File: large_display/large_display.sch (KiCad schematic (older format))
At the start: 128 parts, among them J1 Conn_01x11, J2 Conn_01x11, U1 TLC5940PWP

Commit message: routing: first pass done
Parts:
- gave numbers to parts that had none: 1
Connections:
- net GND: now also C3.2
- net Vdrive: now also C3.1
- net at Df4.1 (K), U1.12 (OUT5): now also Df7.1 (K)
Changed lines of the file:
@@
 $EndComp
 Wire Wire Line
-	2400 1500 2400 1750
+	2400 1500 2400 1600
 $Comp
 L power:GND #PWR0108
@@
 $EndComp
 Wire Wire Line
-	2400 2050 2400 2250
+	2400 2050 2400 2150
 $Comp
 L Device:R R2
@@
 $EndComp
 Wire Wire Line
-	4950 2750 4950 2800
-Wire Wire Line
 	4950 2400 4950 2450
 Wire Wire Line
@@
 	4800 3200 4950 3200
 Wire Wire Line
-	4950 3200 4950 3100
-Wire Wire Line
 	4950 3200 4950 4300
 Wire Wire Line
@@
 	7550 2400 7550 5100
 $Comp
-L Device:C C?
+L Device:C C3
 U 1 1 615CD222
 P 2750 1900
-F 0 "C?" H 2865 1946 50  0000 L CNN
+F 0 "C3" H 2865 1946 50  0000 L CNN
 F 1 "C" H 2865 1855 50  0000 L CNN
 F 2 "Capacitor_SMD:C_0805_2012Metric" H 2788 1750 50  0001 C CNN
@@
 	1    0    0    -1
 $EndComp
+Wire Wire Line
+	2400 1600 2750 1600
+Wire Wire Line
+	2750 1600 2750 1750
+Connection ~ 2400 1600
+Wire Wire Line
+	2400 1600 2400 1750
+Wire Wire Line
+	2400 2150 2750 2150
+Wire Wire Line
+	2750 2150 2750 2050
+Connection ~ 2400 2150
+Wire Wire Line
+	2400 2150 2400 2250
+Wire Wire Line
+	4950 2750 4950 3200
 $EndSCHEMATC

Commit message: Reverse Rg4 Reduce resistor size to 1206 Tidy up tracking Increase track width for VLED Fix text Add revision number
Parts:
- added R17, R22, R37, R39: R, Resistor_SMD:R_1206_3216Metric_Pad1.42x1.75mm_HandSolder, symbol Device:R
- C1, C3: value C -> 100n
- C2: value CP -> 10u
- R10, R11, R12, R13, R14, R15, R16, R3, R4, R5, R6, R7, R8, R9: footprint Resistor_SMD:R_1812_4532Metric_Pad1.30x3.40mm_HandSolder -> Resistor_SMD:R_1206_3216Metric_Pad1.42x1.75mm_HandSolder
- R18: renamed from R17; footprint Resistor_SMD:R_1812_4532Metric_Pad1.30x3.40mm_HandSolder -> Resistor_SMD:R_1206_3216Metric_Pad1.42x1.75mm_HandSolder
- R19: renamed from R18; footprint Resistor_SMD:R_1812_4532Metric_Pad1.30x3.40mm_HandSolder -> Resistor_SMD:R_1206_3216Metric_Pad1.42x1.75mm_HandSolder
- R2: value R -> 100k
- R20: renamed from R19; footprint Resistor_SMD:R_1812_4532Metric_Pad1.30x3.40mm_HandSolder -> Resistor_SMD:R_1206_3216Metric_Pad1.42x1.75mm_HandSolder
- R21: renamed from R20; footprint Resistor_SMD:R_1812_4532Metric_Pad1.30x3.40mm_HandSolder -> Resistor_SMD:R_1206_3216Metric_Pad1.42x1.75mm_HandSolder
- R23: renamed from R21; footprint Resistor_SMD:R_1812_4532Metric_Pad1.30x3.40mm_HandSolder -> Resistor_SMD:R_1206_3216Metric_Pad1.42x1.75mm_HandSolder
- R24: renamed from R22; footprint Resistor_SMD:R_1812_4532Metric_Pad1.30x3.40mm_HandSolder -> Resistor_SMD:R_1206_3216Metric_Pad1.42x1.75mm_HandSolder
- R25: renamed from R23; footprint Resistor_SMD:R_1812_4532Metric_Pad1.30x3.40mm_HandSolder -> Resistor_SMD:R_1206_3216Metric_Pad1.42x1.75mm_HandSolder
- R26: renamed from R24; footprint Resistor_SMD:R_1812_4532Metric_Pad1.30x3.40mm_HandSolder -> Resistor_SMD:R_1206_3216Metric_Pad1.42x1.75mm_HandSolder
- R27: renamed from R25; footprint Resistor_SMD:R_1812_4532Metric_Pad1.30x3.40mm_HandSolder -> Resistor_SMD:R_1206_3216Metric_Pad1.42x1.75mm_HandSolder
- R28: renamed from R26; footprint Resistor_SMD:R_1812_4532Metric_Pad1.30x3.40mm_HandSolder -> Resistor_SMD:R_1206_3216Metric_Pad1.42x1.75mm_HandSolder
- R29: renamed from R27; footprint Resistor_SMD:R_1812_4532Metric_Pad1.30x3.40mm_HandSolder -> Resistor_SMD:R_1206_3216Metric_Pad1.42x1.75mm_HandSolder
- R30: renamed from R28; footprint Resistor_SMD:R_1812_4532Metric_Pad1.30x3.40mm_HandSolder -> Resistor_SMD:R_1206_3216Metric_Pad1.42x1.75mm_HandSolder
- R31: renamed from R29; footprint Resistor_SMD:R_1812_4532Metric_Pad1.30x3.40mm_HandSolder -> Resistor_SMD:R_1206_3216Metric_Pad1.42x1.75mm_HandSolder
- R32: renamed from R30; footprint Resistor_SMD:R_1812_4532Metric_Pad1.30x3.40mm_HandSolder -> Resistor_SMD:R_1206_3216Metric_Pad1.42x1.75mm_HandSolder
- R33: renamed from R31; footprint Resistor_SMD:R_1812_4532Metric_Pad1.30x3.40mm_HandSolder -> Resistor_SMD:R_1206_3216Metric_Pad1.42x1.75mm_HandSolder
- R34: renamed from R32; footprint Resistor_SMD:R_1812_4532Metric_Pad1.30x3.40mm_HandSolder -> Resistor_SMD:R_1206_3216Metric_Pad1.42x1.75mm_HandSolder
- R35: renamed from R33; footprint Resistor_SMD:R_1812_4532Metric_Pad1.30x3.40mm_HandSolder -> Resistor_SMD:R_1206_3216Metric_Pad1.42x1.75mm_HandSolder
- R36: renamed from R34; footprint Resistor_SMD:R_1812_4532Metric_Pad1.30x3.40mm_HandSolder -> Resistor_SMD:R_1206_3216Metric_Pad1.42x1.75mm_HandSolder
- R38: renamed from R35; footprint Resistor_SMD:R_1812_4532Metric_Pad1.30x3.40mm_HandSolder -> Resistor_SMD:R_1206_3216Metric_Pad1.42x1.75mm_HandSolder
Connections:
- net Vdrive: now also R17.1; no longer R18.1
- net at R20.2, U1.14 (OUT7): now also R22.2; no longer R21.2
- net at Dg3.2 (A), R18.2: now also Dg4.1 (K); no longer Dg4.2 (A)
- net at R19.1: now also Dg4.2 (A); no longer Dg4.1 (K)
- net at R36.2: now also R37.1; no longer Dn3.2 (A)
- net at R38.2: now also R39.1; no longer Dp1.2 (A)
- new net: R17.2, R18.1
- new net: Dn3.2 (A), R37.2
- new net: Dp1.2 (A), R39.2
- new net: R21.2, R22.1
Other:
- moved on the sheet: Dg3, Dg4, Dn3, Dp1, R16, R18, R19, R20, R21

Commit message: Add buffering for passthru signals More tidying up of tracking
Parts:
- added U2: 74HC244, symbol 74xx:74HC244
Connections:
- net GND: now also U2.1 (1OE), U2.10 (GND), U2.19 (2OE), U2.4 (1A1), U2.6 (1A2)
- net VCC: now also U2.20 (VCC)
- net at J2.5 (Pin_5), U1.2 (BLANK): now also U2.17 (2A0); no longer J1.5 (Pin_5)
- net at J2.4 (Pin_4), U1.25 (GSCLK): now also U2.8 (1A3); no longer J1.4 (Pin_4)
- net at J2.1 (Pin_1), R2.2, U1.26 (DCPRG): now also U2.2 (1A0); no longer J1.1 (Pin_1)
- net at J2.6 (Pin_6), U1.3 (XLAT): now also U2.15 (2A1); no longer J1.6 (Pin_6)
- net at J2.7 (Pin_7), U1.4 (SCLK): now also U2.13 (2A2); no longer J1.7 (Pin_7)
- net at U1.5 (SIN): now also U2.11 (2A3); no longer J1.8 (Pin_8)
- new net: J1.1 (Pin_1), U2.18 (1Y0)
- new net: J1.4 (Pin_4), U2.12 (1Y3)
- new net: J1.5 (Pin_5), U2.3 (2Y0)
- new net: J1.6 (Pin_6), U2.5 (2Y1)
- new net: J1.7 (Pin_7), U2.7 (2Y2)
- new net: J1.8 (Pin_8), U2.9 (2Y3)
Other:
- moved on the sheet: J1
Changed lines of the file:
@@
 $EndComp
-Wire Wire Line
-	9050 2950 8950 2950
 Wire Wire Line
 	8800 4900 9050 4900
@@
 L power:VCC #PWR010
 U 1 1 5FBCAFFD
-P 8700 1750
-F 0 "#PWR010" H 8700 1600 50  0001 C CNN
-F 1 "VCC" H 8717 1923 50  0000 C CNN
-F 2 "" H 8700 1750 50  0001 C CNN
-F 3 "" H 8700 1750 50  0001 C CNN
-	1    8700 1750
+P 8700 1400
+F 0 "#PWR010" H 8700 1250 50  0001 C CNN
+F 1 "VCC" H 8717 1573 50  0000 C CNN
+F 2 "" H 8700 1400 50  0001 C CNN
+F 3 "" H 8700 1400 50  0001 C CNN
+	1    8700 1400
 	1    0    0    -1
 $EndComp
@@
 L power:Vdrive #PWR011
 U 1 1 5FBCC6DE
-P 8950 1750
-F 0 "#PWR011" H 8750 1600 50  0001 C CNN
-F 1 "Vdrive" H 8967 1923 50  0000 C CNN
-F 2 "" H 8950 1750 50  0001 C CNN
-F 3 "" H 8950 1750 50  0001 C CNN
-	1    8950 1750
+P 8800 1150
+F 0 "#PWR011" H 8600 1000 50  0001 C CNN
+F 1 "Vdrive" H 8817 1323 50  0000 C CNN
+F 2 "" H 8800 1150 50  0001 C CNN
+F 3 "" H 8800 1150 50  0001 C CNN
+	1    8800 1150
 	1    0    0    -1
 $EndComp
@@
 L Connector_Generic:Conn_01x11 J1
 U 1 1 5FC1A142
-P 9250 2450
-F 0 "J1" H 9330 2492 50  0000 L CNN
-F 1 "Conn_01x11" H 9330 2401 50  0000 L CNN
-F 2 "Connector_PinHeader_2.54mm:PinHeader_1x11_P2.54mm_Horizontal" H 9250 2450 50  0001 C CNN
-F 3 "~" H 9250 2450 50  0001 C CNN
-	1    9250 2450
+P 10600 2450
+F 0 "J1" H 10680 2492 50  0000 L CNN
+F 1 "Conn_01x11" H 10680 2401 50  0000 L CNN
+F 2 "Connector_PinHeader_2.54mm:PinHeader_1x11_P2.54mm_Horizontal" H 10600 2450 50  0001 C CNN
+F 3 "~" H 10600 2450 50  0001 C CNN
+	1    10600 2450
 	1    0    0    -1
 $EndComp
@@
 $EndComp
 Wire Wire Line
-	8950 1750 8950 2950
-Wire Wire Line
-	9050 2850 8750 2850
-Wire Wire Line
-	8750 2850 8750 4800
-Wire Wire Line
-	8800 2950 8800 4900
-Wire Wire Line
-	9050 2750 8700 2750
-Wire Wire Line
-	8700 2750 8700 4700
-Wire Wire Line
 	8700 4700 9050 4700
 Wire Wire Line
-	9050 2550 8550 2550
-Wire Wire Line
 	8550 2550 8550 4500
 Wire Wire Line
 	8550 4500 9050 4500
 Wire Wire Line
-	9050 2450 8500 2450
-Wire Wire Line
 	8500 2450 8500 4400
 Wire Wire Line
 	8500 4400 9050 4400
 Wire Wire Line
-	9050 2350 8450 2350
-Wire Wire Line
 	8450 2350 8450 4300
 Wire Wire Line
 	8450 4300 9050 4300
 Wire Wire Line
-	9050 2250 8400 2250
-Wire Wire Line
 	8400 2250 8400 4200
 Wire Wire Line
 	8400 4200 9050 4200
 Wire Wire Line
-	9050 2150 8350 2150
-Wire Wire Line
-	8350 2150 8350 4100
-Wire Wire Line
 	8350 4100 9050 4100
 Wire Wire Line
-	9050 2050 8300 2050
-Wire Wire Line
 	8300 4000 9050 4000
 Wire Wire Line
-	9050 1950 8250 1950
-Wire Wire Line
 	8250 1950 8250 3900
 Wire Wire Line
 	8250 3900 9050 3900
-Connection ~ 8950 2950
-Wire Wire Line
-	8950 2950 8800 2950
-Wire Wire Line
-	8700 1750 8700 2750
-Connection ~ 8700 2750
 Wire Wire Line
 	9050 4600 8650 4600
@@
 Wire Wire Line
 	3050 5850 8600 5850
-Wire Wire Line
-	8600 2650 9050 2650
 Wire Wire Line
 	8550 4500 8550 5900
@@
 Wire Wire Line
 	8300 4000 8300 6150
-Wire Wire Line
-	8300 2050 8300 4000
 Wire Wire Line
 	7850 1300 8000 1300
@@
 Wire Wire Line
 	5750 4250 5750 4500
+$Comp
+L 74xx:74HC244 U2
+U 1 1 60667868
+P 9650 2450
+F 0 "U2" H 9400 3150 50  0000 C CNN
+F 1 "74HC244" H 9900 1750 50  0000 C CNN
+F 2 "" H 9650 2450 50  0001 C CNN
+F 3 "https://assets.nexperia.com/documents/data-sheet/74HC_HCT244.pdf" H 9650 2450 50  0001 C CNN
+	1    9650 2450
+	1    0    0    -1
+$EndComp
+Wire Wire Line
+	8700 1400 8700 3400
+Wire Wire Line
+	8800 1150 8800 3500
+$Comp
+L power:VCC #PWR013
+U 1 1 607D19C3
+P 9650 1400
+F 0 "#PWR013" H 9650 1250 50  0001 C CNN
+F 1 "VCC" H 9667 1573 50  0000 C CNN
+F 2 "" H 9650 1400 50  0001 C CNN
+F 3 "" H 9650 1400 50  0001 C CNN
+	1    9650 1400
+	1    0    0    -1
+$EndComp
+$Comp
+L power:GND #PWR014
+U 1 1 607D32AB
+P 9650 3700
+F 0 "#PWR014" H 9650 3450 50  0001 C CNN
+F 1 "GND" H 9655 3527 50  0000 C CNN
+F 2 "" H 9650 3700 50  0001 C CNN
+F 3 "" H 9650 3700 50  0001 C CNN
+	1    9650 3700
+	1    0    0    -1
+$EndComp
+Wire Wire Line
+	9650 3700 9650 3300
+Wire Wire Line
+	9650 1650 9650 1400
+Wire Wire Line
+	9150 2650 8600 2650
+Wire Wire Line
+	9150 2550 8550 2550
+Wire Wire Line
+	9150 2450 8500 2450
+Wire Wire Line
+	9150 2350 8450 2350
+Wire Wire Line
+	9150 2250 8400 2250
+Wire Wire Line
+	9150 2850 9050 2850
+Wire Wire Line
+	9050 2850 9050 2950
+Wire Wire Line
+	9050 3300 9650 3300
+Connection ~ 9650 3300
+Wire Wire Line
+	9650 3300 9650 3250
+Wire Wire Line
+	9150 2950 9050 2950
+Connection ~ 9050 2950
+Wire Wire Line
+	9050 2950 9050 3300
+Wire Wire Line
+	8250 1950 9150 1950
+Wire Wire Line
+	10150 1950 10400 1950
+Wire Wire Line
+	8300 1500 10350 1500
+Wire Wire Line
+	10350 1500 10350 2050
+Wire Wire Line
+	10350 2050 10400 2050
+Wire Wire Line
+	8300 1500 8300 4000
+Wire Wire Line
+	10400 2150 10300 2150
+Wire Wire Line
+	10300 2150 10300 1550
+Wire Wire Line
+	10300 1550 8350 1550
+Wire Wire Line
+	8350 1550 8350 4100
+Wire Wire Line
+	9150 2050 9050 2050
+Wire Wire Line
+	9050 2050 9050 2150
+Connection ~ 9050 2850
+Wire Wire Line
+	9150 2150 9050 2150
+Connection ~ 9050 2150
+Wire Wire Line
+	9050 2150 9050 2850
+Wire Wire Line
+	10400 2750 10150 2750
+Wire Wire Line
+	10150 2750 10150 3400
+Wire Wire Line
+	10150 3400 8700 3400
+Connection ~ 8700 3400
+Wire Wire Line
+	8700 3400 8700 4700
+Wire Wire Line
+	10400 2850 10200 2850
+Wire Wire Line
+	10200 2850 10200 3450
+Wire Wire Line
+	10200 3450 8750 3450
+Wire Wire Line
+	8750 3450 8750 4800
+Wire Wire Line
+	10400 2950 10250 2950
+Wire Wire Line
+	10250 2950 10250 3500
+Wire Wire Line
+	10250 3500 8800 3500
+Connection ~ 8800 3500
+Wire Wire Line
+	8800 3500 8800 4900
+Wire Wire Line
+	10400 2250 10150 2250
+Wire Wire Line
+	10150 2350 10400 2350
+Wire Wire Line
+	10400 2450 10150 2450
+Wire Wire Line
+	10150 2550 10400 2550
+Wire Wire Line
+	10400 2650 10150 2650
 $EndSCHEMATC

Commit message: add decoupling for buffer IC
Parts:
- added C4: 100n, Capacitor_SMD:C_0805_2012Metric, symbol Device:C
- U2: footprint (none) -> Package_SO:SSOP-20_5.3x7.2mm_P0.65mm
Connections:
- net GND: now also C4.2
- net VCC: now also C4.1
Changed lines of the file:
@@
 encoding utf-8
 Sheet 1 1
-Title ""
-Date ""
-Rev ""
+Title "Large Display"
+Date "2020-11-28"
+Rev "0.2"
 Comp ""
-Comment1 ""
-Comment2 ""
+Comment1 "https://github.com/nes0/large-display"
+Comment2 "SPDX-License-Identifier:  CERN-OHL-W-2.0"
 Comment3 ""
 Comment4 ""
@@
 	2300 4500 2300 4700
 Wire Wire Line
-	2000 2050 2000 2250
+	2000 2050 2000 2150
 $Comp
 L power:VCC #PWR01
@@
 $EndComp
 Wire Wire Line
-	2000 1500 2000 1750
+	2000 1500 2000 1600
 $Comp
 L Device:CP C2
@@
 F 0 "U2" H 9400 3150 50  0000 C CNN
 F 1 "74HC244" H 9900 1750 50  0000 C CNN
-F 2 "" H 9650 2450 50  0001 C CNN
+F 2 "Package_SO:SSOP-20_5.3x7.2mm_P0.65mm" H 9650 2450 50  0001 C CNN
 F 3 "https://assets.nexperia.com/documents/data-sheet/74HC_HCT244.pdf" H 9650 2450 50  0001 C CNN
 	1    9650 2450
@@
 Wire Wire Line
 	10400 2650 10150 2650
+$Comp
+L Device:C C4
+U 1 1 60E9B274
+P 1500 1900
+F 0 "C4" H 1615 1946 50  0000 L CNN
+F 1 "100n" H 1615 1855 50  0000 L CNN
+F 2 "Capacitor_SMD:C_0805_2012Metric" H 1538 1750 50  0001 C CNN
+F 3 "~" H 1500 1900 50  0001 C CNN
+	1    1500 1900
+	1    0    0    -1
+$EndComp
+Wire Wire Line
+	2000 1600 1500 1600
+Wire Wire Line
+	1500 1600 1500 1750
+Connection ~ 2000 1600
+Wire Wire Line
+	2000 1600 2000 1750
+Wire Wire Line
+	1500 2050 1500 2150
+Wire Wire Line
+	1500 2150 2000 2150
+Connection ~ 2000 2150
+Wire Wire Line
+	2000 2150 2000 2250
 $EndSCHEMATC

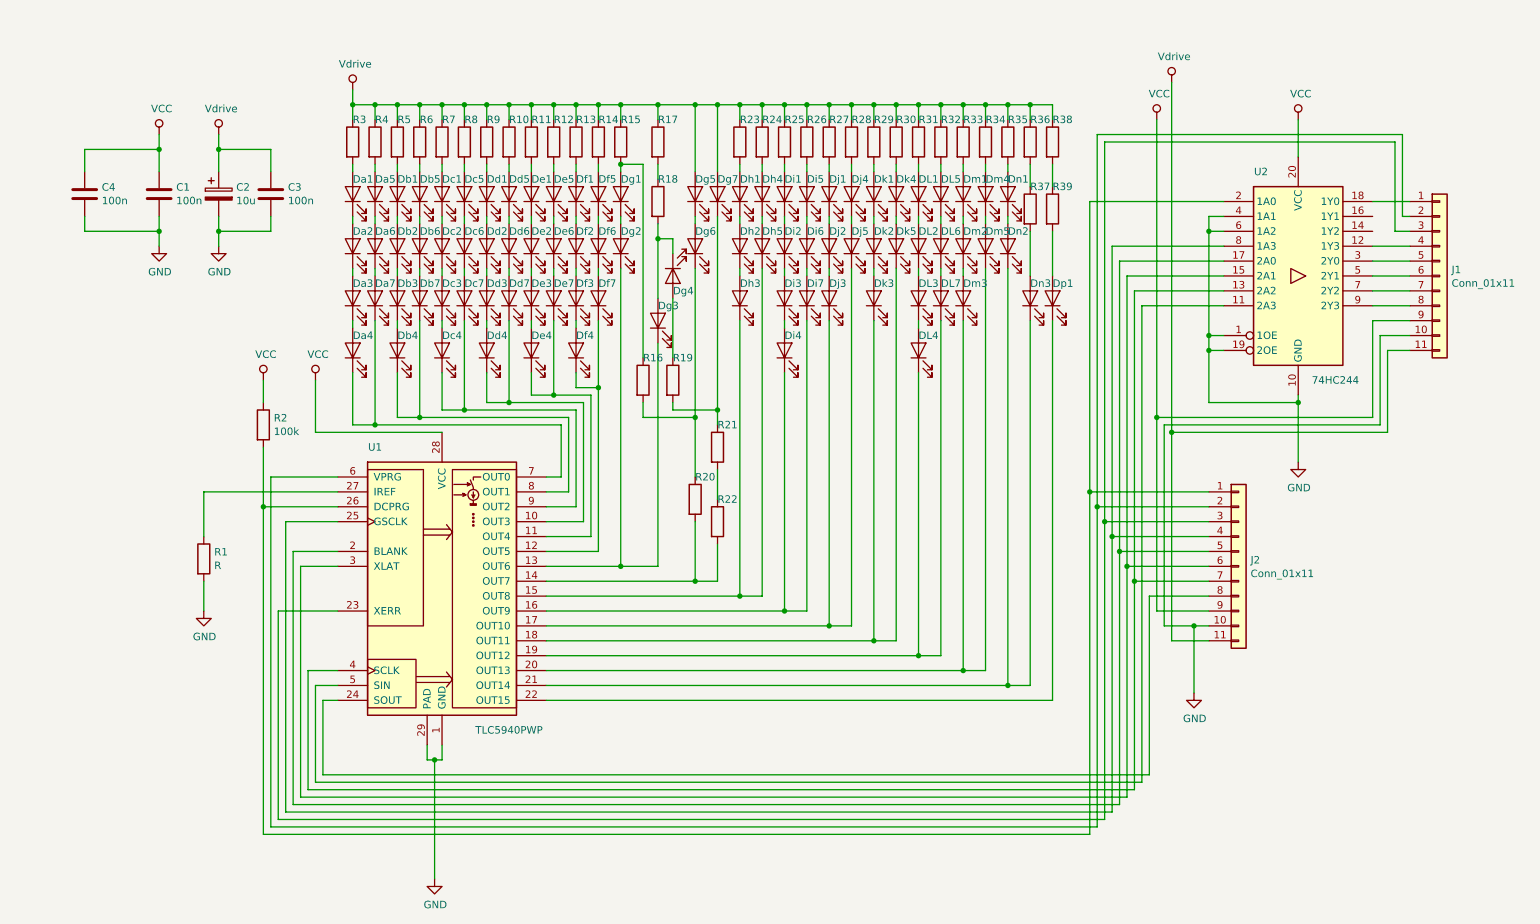
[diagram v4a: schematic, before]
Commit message: add a bit of clearance between segment outlines and nearest components for light dam
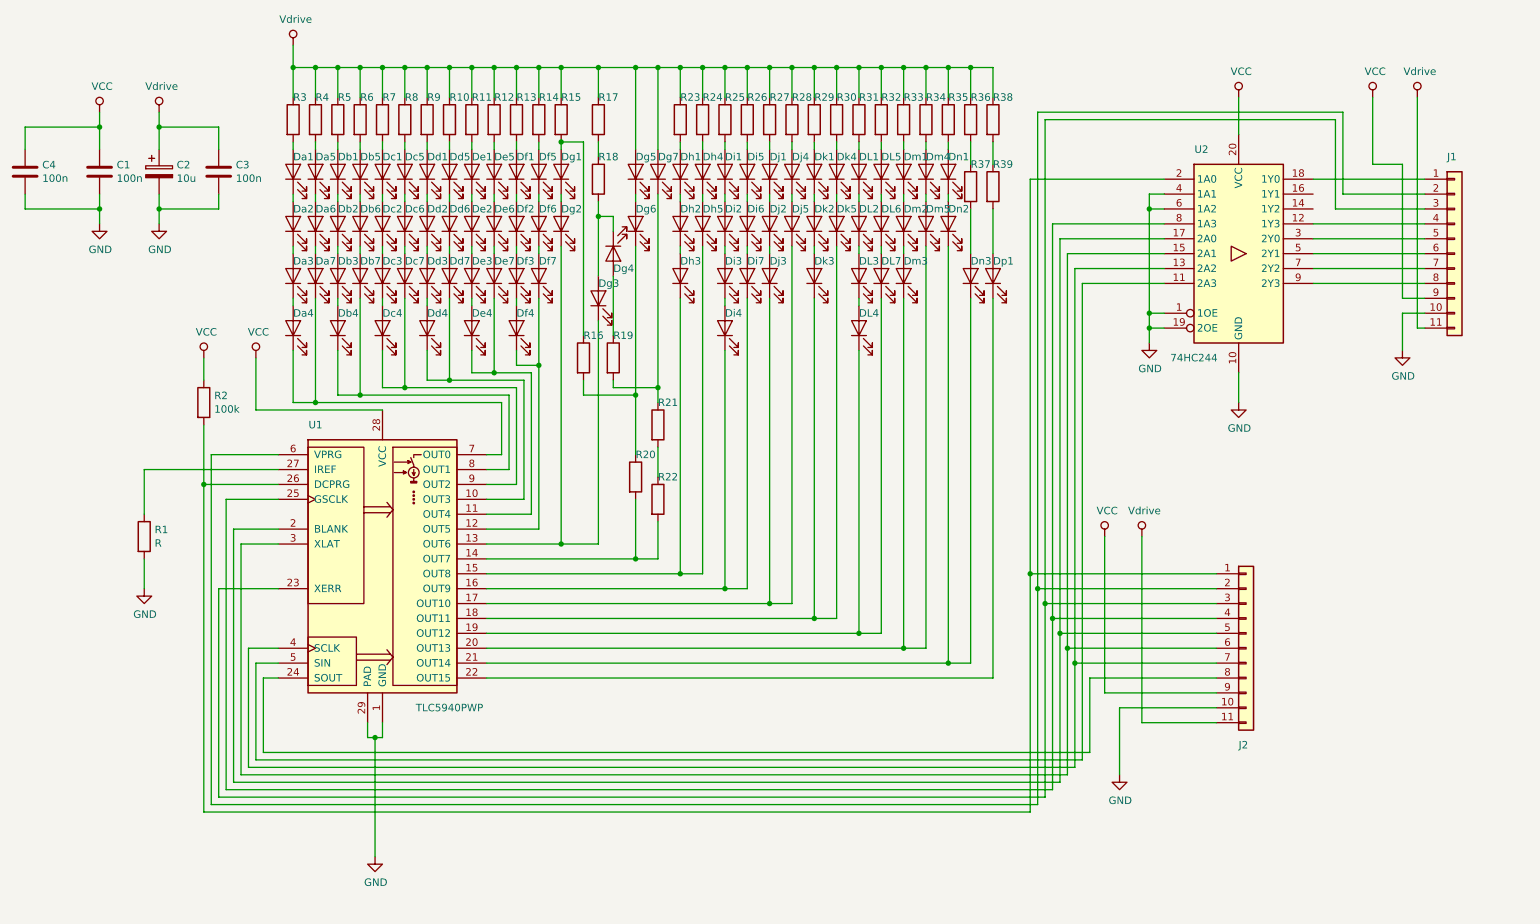
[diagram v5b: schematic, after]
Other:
- moved on the sheet: C1, C2, C3, C4, DL1, DL2, DL3, DL4, DL5, DL6, DL7, Da1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
